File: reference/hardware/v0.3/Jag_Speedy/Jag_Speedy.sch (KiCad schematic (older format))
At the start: 19 parts, among them U1 LMV324, U2 LMV324, U3 Teensy 3.5

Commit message: Schematic pin mapping
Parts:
- added R84, R85, R90, R91: 180k, Resistor_THT:R_Axial_DIN0207_L6.3mm_D2.5mm_P2.54mm_Vertical, symbol Device:R
- added R86, R87, R88, R89: 330k, Resistor_THT:R_Axial_DIN0207_L6.3mm_D2.5mm_P2.54mm_Vertical, symbol Device:R
- added U4: LMV324, Package_DIP:DIP-14_W7.62mm_Socket, symbol Amplifier_Operational:LMV324
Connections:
- net SignalGnd: now also R86.2, R87.2, R88.1, R89.1
- net CPU-D24: now reaches U3.16 (24)
- net CPU-D25: now reaches U3.17 (25)
- net CPU-D29: now reaches U3.21 (29_PWM_CAN0TX_Touch)
- net CPU-D13: now reaches U3.40 (13_SCK0_LED)
- net CAN-Tx: now reaches U3.5 (3_PWM_CAN0TX_SCL2)
- net CAN-Rx: now reaches U3.6 (4_PWM_CAN0RX_SDA2)
- net BRV-A4-3.3V renamed CPU-A4
- net Barro-A5-3.3V renamed Barro-Signal-3.3V
- net Barro-Signal-3.3V: no longer U3.46 (19_A5_SCL0_Touch)
- net Barro-A5-5V renamed Barro-Signal-5V
- net BoostPWM-CPU-A21: no longer names the net of U3.37 (A21_DAC0)
- net CLT-A1-3.3V renamed CLT-Signal-3.3V
- net CLT-Signal-3.3V: no longer U3.42 (15_A1_CS0_Touch)
- net CLT-A1-5V renamed CLT-Signal-5V
- net ClutchIn-CPU-D51: no longer names the net of U3.79 (51_MISO2)
- net FPress-A10-3.3V renamed FPress-Signal-3.3V
- net FPress-Signal-3.3V: no longer U3.56 (A10)
- net FPress-A10-5V renamed FPress-Signal-5V
- net Fan-CPU-D27 renamed CPU-D27
- net FlexFuel: no longer names the net of U3.4 (2_PWM)
- net FuelPump-CPU-D37 renamed CPU-D37
- net IAT-A0-3.3V renamed IAT-Signal-3.3V
- net IAT-Signal-3.3V: no longer U3.41 (14_A0_PWM_SCK0)
- net IAT-A0-5V renamed IAT-Signal-5V
- net Idle02 renamed CPU-D06
- net IdlePWM-CPU-D05 renamed CPU-D05
- net Ign01-CPU-D39 renamed CPU-D39
- net Ign02-CPU-D38 renamed CPU-D38
- net Ign03-CPU-D31 renamed CPU-D31
- net Ign04-CPU-D21 renamed CPU-D21
- net Ign05-CPU-D32 renamed CPU-D32
- net Ign06-CPU-D35 renamed CPU-D35
- net Inj01-CPU-D08 renamed CPU-D08
- net Inj02-CPU-D09 renamed CPU-D09
- net Inj03-CPU-D10 renamed CPU-D10
- net Inj04-CPU-D11 renamed CPU-D11
- net Inj05-CPU-D12 renamed CPU-D12
- net Inj06-CPU-D07 renamed CPU-D07
- net MAP-A3-3.3V renamed MAP-Signal-3.3V
- net MAP-Signal-3.3V: no longer U3.44 (17_A3_SDA0_Touch)
- net MAP-A3-5V renamed MAP-Signal-5V
- net O2-A8-3.3V renamed O2-Signal-3.3V
- net O2-Signal-3.3V: no longer U3.49 (22_A8_PWM_Touch)
- net O2-A8-5V renamed O2-Signal-5V
- net OPress-A11-3.3V renamed OPress-Signal-3.3V
- net OPress-Signal-3.3V: no longer U3.57 (A11)
- net OPress-A11-5V renamed OPress-Signal-5V
- net TPS-A2-3.3V renamed TPS-Signal-3.3V
- net TPS-Signal-3.3V: no longer U3.43 (16_A2_SCL0_Touch)
- net TPS-A2-5V renamed TPS-Signal-5V
- net TachoOut-CPU-D28 renamed CPU-D28
- net VVT: no longer names the net of U3.38 (A22_DAC1)
- new net: R88.2, R90.1, U4.3 (+)
- new net: R85.2, R87.1, U4.12 (+)
- new net: R89.2, R91.1, U4.10 (+)
- new net: R84.2, R86.1, U4.5 (+)
- new net BRV-Signal-3.3V: U4.6 (-), U4.7
- new net BRV-Signal-5V: R84.1
- new net CPU-A0: U3.41 (14_A0_PWM_SCK0)
- new net CPU-A1: U3.42 (15_A1_CS0_Touch)
- new net CPU-A10: U3.56 (A10)
- new net CPU-A11: U3.57 (A11)
- new net CPU-A2: U3.43 (16_A2_SCL0_Touch)
- new net CPU-A3: U3.44 (17_A3_SDA0_Touch)
- new net CPU-A5: U3.46 (19_A5_SCL0_Touch)
- new net CPU-A8: U3.49 (22_A8_PWM_Touch)
- new net Spare-Signal-3.3V-01: U4.1, U4.2 (-)
- new net Spare-Signal-3.3V-02: U4.13 (-), U4.14
- new net Spare-Signal-3.3V-03: U4.8, U4.9 (-)
- new net Spare-Signal-5V-01: R90.2
- new net Spare-Signal-5V-02: R85.1
- new net Spare-Signal-5V-03: R91.2
- no-connect marks 43 -> 44
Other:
- moved on the sheet: R11, R12, R15, R16, R3, R4, R7, R8, U1E, U2A, U2B, U2C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

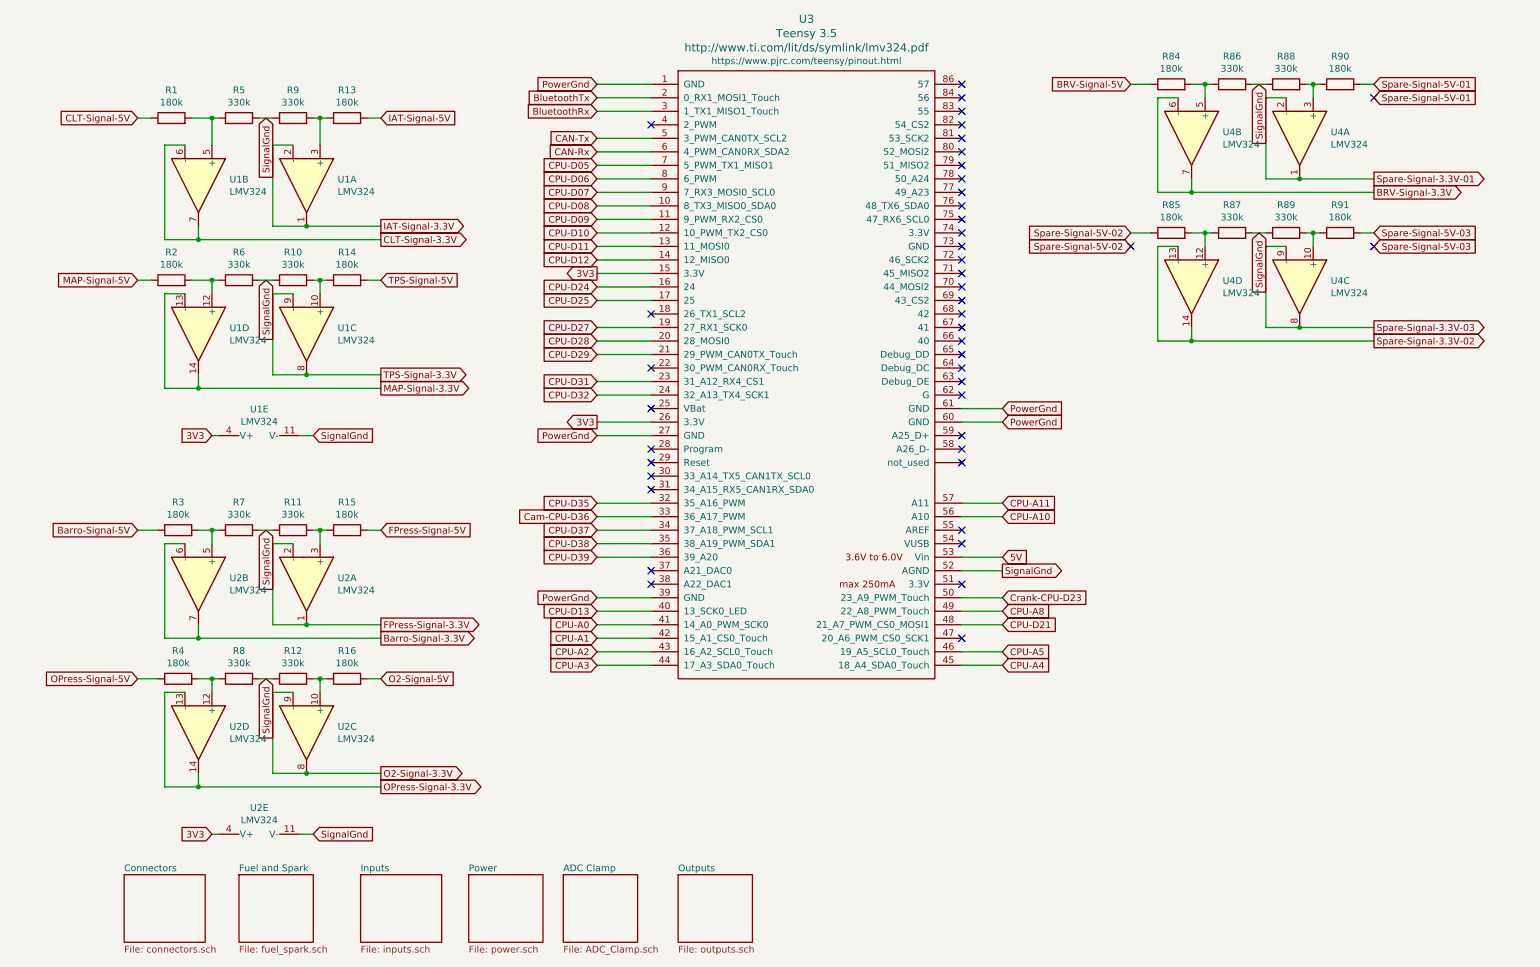
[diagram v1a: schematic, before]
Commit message: Canbus Tranceiver
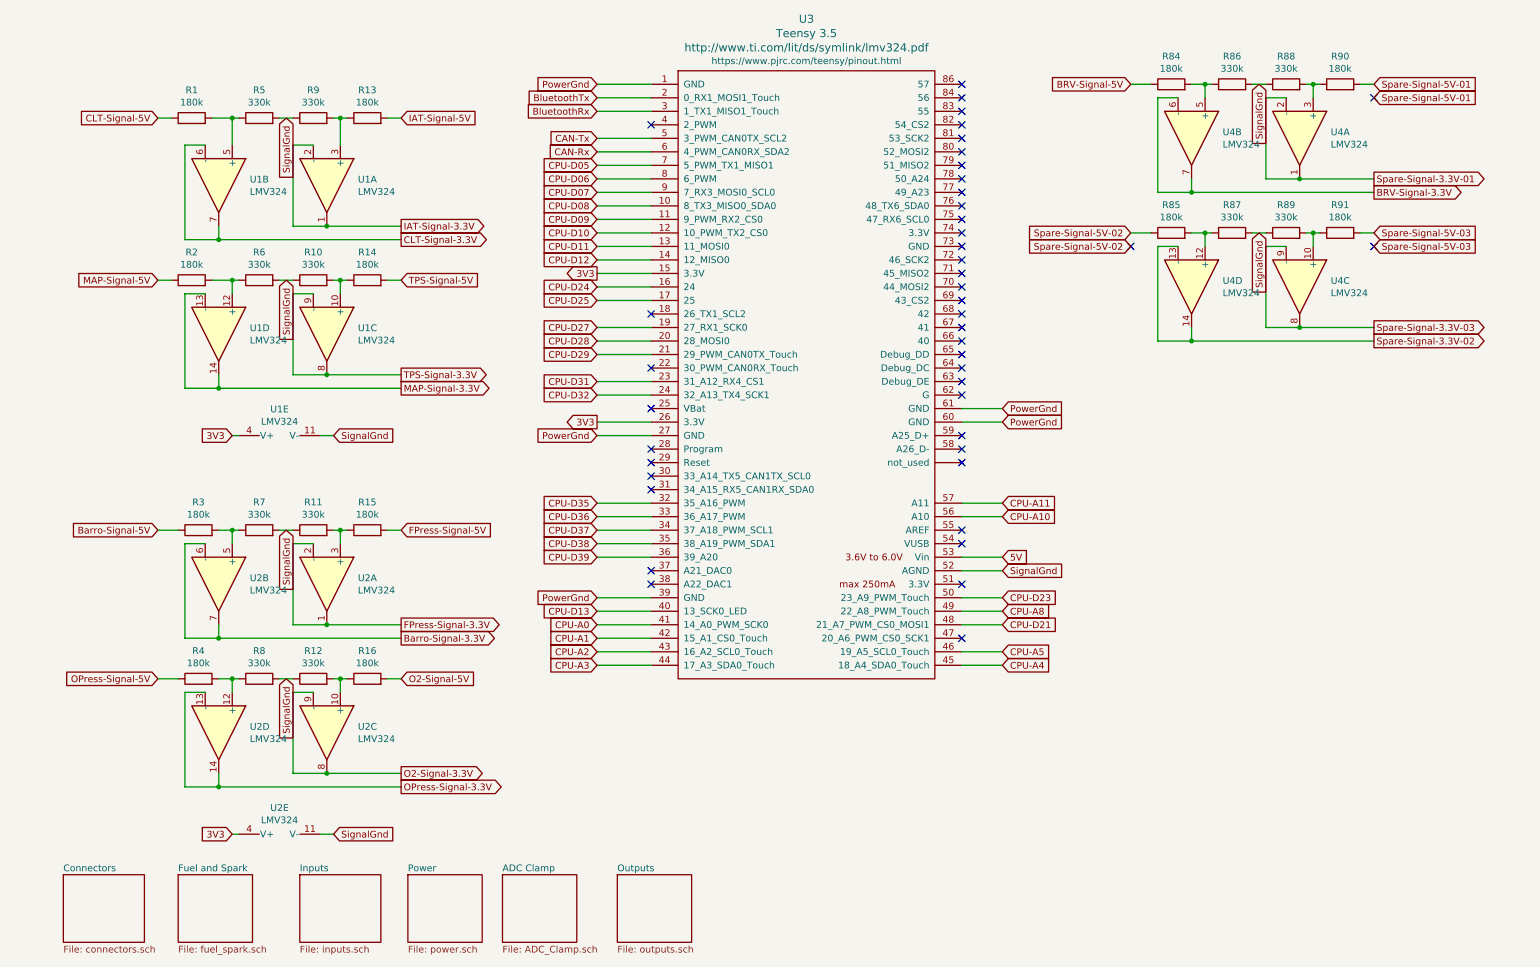
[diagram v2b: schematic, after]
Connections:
- net Cam-CPU-D36 renamed CPU-D36
- net Crank-CPU-D23 renamed CPU-D23
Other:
- moved on the sheet: R1, R10, R11, R12, R13, R14, R15, R16, R2, R3, R4, R5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

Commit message: MOSFET Drivers
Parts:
- U3: symbol Teensy:Teensy3.5 -> Jag_Speedy-rescue:Teensy3.5-Teensy
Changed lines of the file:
@@
 NoConn ~ 4900 1450
 $Comp
-L Teensy:Teensy3.5 U3
+L Jag_Speedy-rescue:Teensy3.5-Teensy U3
 U 1 1 5EEF3E22
 P 6050 3300

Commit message: Rationalise level shifting
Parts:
- removed R1, R13, R14, R15, R16, R2, R3, R4, R84, R85, R90, R91: 180k, Resistor_THT:R_Axial_DIN0207_L6.3mm_D2.5mm_P2.54mm_Vertical, symbol Device:R
- removed R10, R11, R12, R5, R6, R7, R8, R86, R87, R88, R89, R9: 330k, Resistor_THT:R_Axial_DIN0207_L6.3mm_D2.5mm_P2.54mm_Vertical, symbol Device:R
- removed U1, U2, U4: LMV324, Package_DIP:DIP-14_W7.62mm_Socket, symbol Amplifier_Operational:LMV324
- U3: symbol Jag_Speedy-rescue:Teensy3.5-Teensy -> Jag_Speedy-rescue:Teensy3.5-Teensy-Jag_Speedy-rescue
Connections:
- no-connect marks 44 -> 41

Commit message: SMD Update
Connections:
- net Reset: now reaches U3.29 (Reset)
- no-connect marks 41 -> 40
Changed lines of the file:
@@
 NoConn ~ 4900 3550
 NoConn ~ 4900 3850
-NoConn ~ 4900 3950
 NoConn ~ 7200 1150
 NoConn ~ 7200 1250
@@
 Wire Wire Line
 	4900 2750 4500 2750
+Text GLabel 4500 3950 0    50   Input ~ 0
+Reset
+Wire Wire Line
+	4900 3950 4500 3950
 $EndSCHEMATC
